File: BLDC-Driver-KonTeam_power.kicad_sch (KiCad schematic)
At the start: 73 parts, among them J1 Mode_HOA, J10 Mode_HOB, J11 Mode_LOB, J12 A, J13 B, J14 C, J2 BUck, J3 Logic_Conn, J4 Logic_Test, J5 Gate_Test, J6 IN, J7 Mode_LOC, J8 Mode_HOC, J9 Mode_LOA, Q1 IRFZ44N, Q10 IRFZ44N, Q11 IRFZ44N, Q12 IRFZ44N, Q2 IRFZ44N, Q3 IRFZ44N, Q4 IRFZ44N, Q5 IRFZ44N, Q6 IRFZ44N, Q7 IRFZ44N, Q8 IRFZ44N, Q9 IRFZ44N, U1 IR2101, U2 IR2101, U3 IR2101, U4 LM7805_TO220

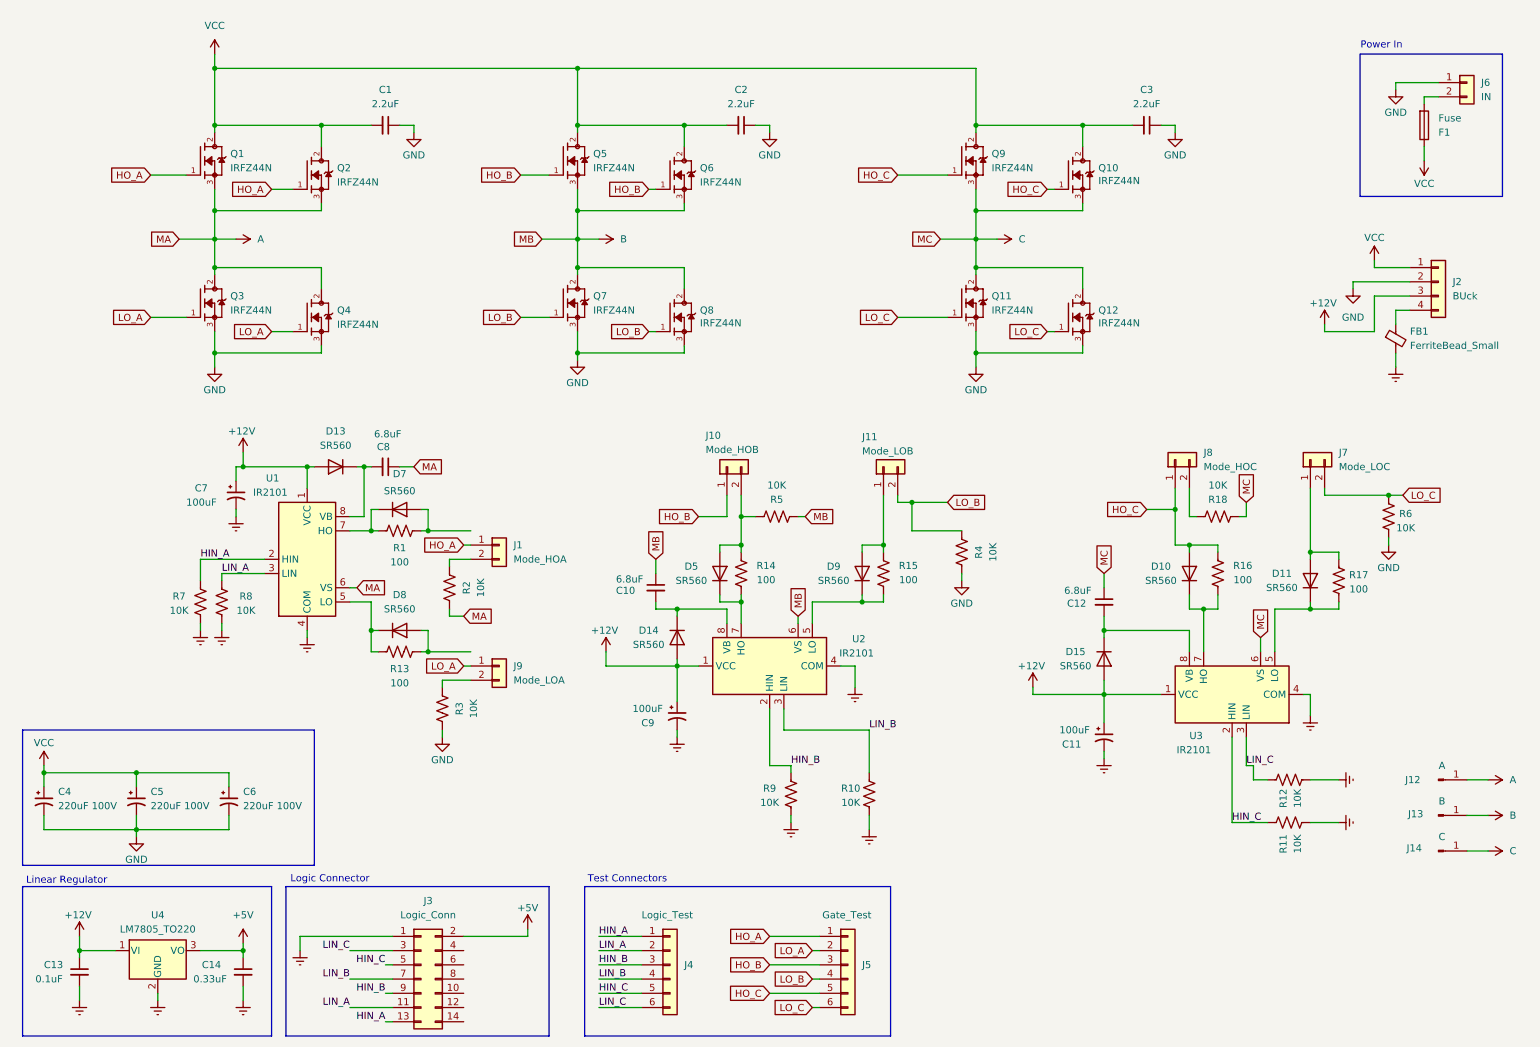
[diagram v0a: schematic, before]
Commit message: Formato Gate Drivers Enable
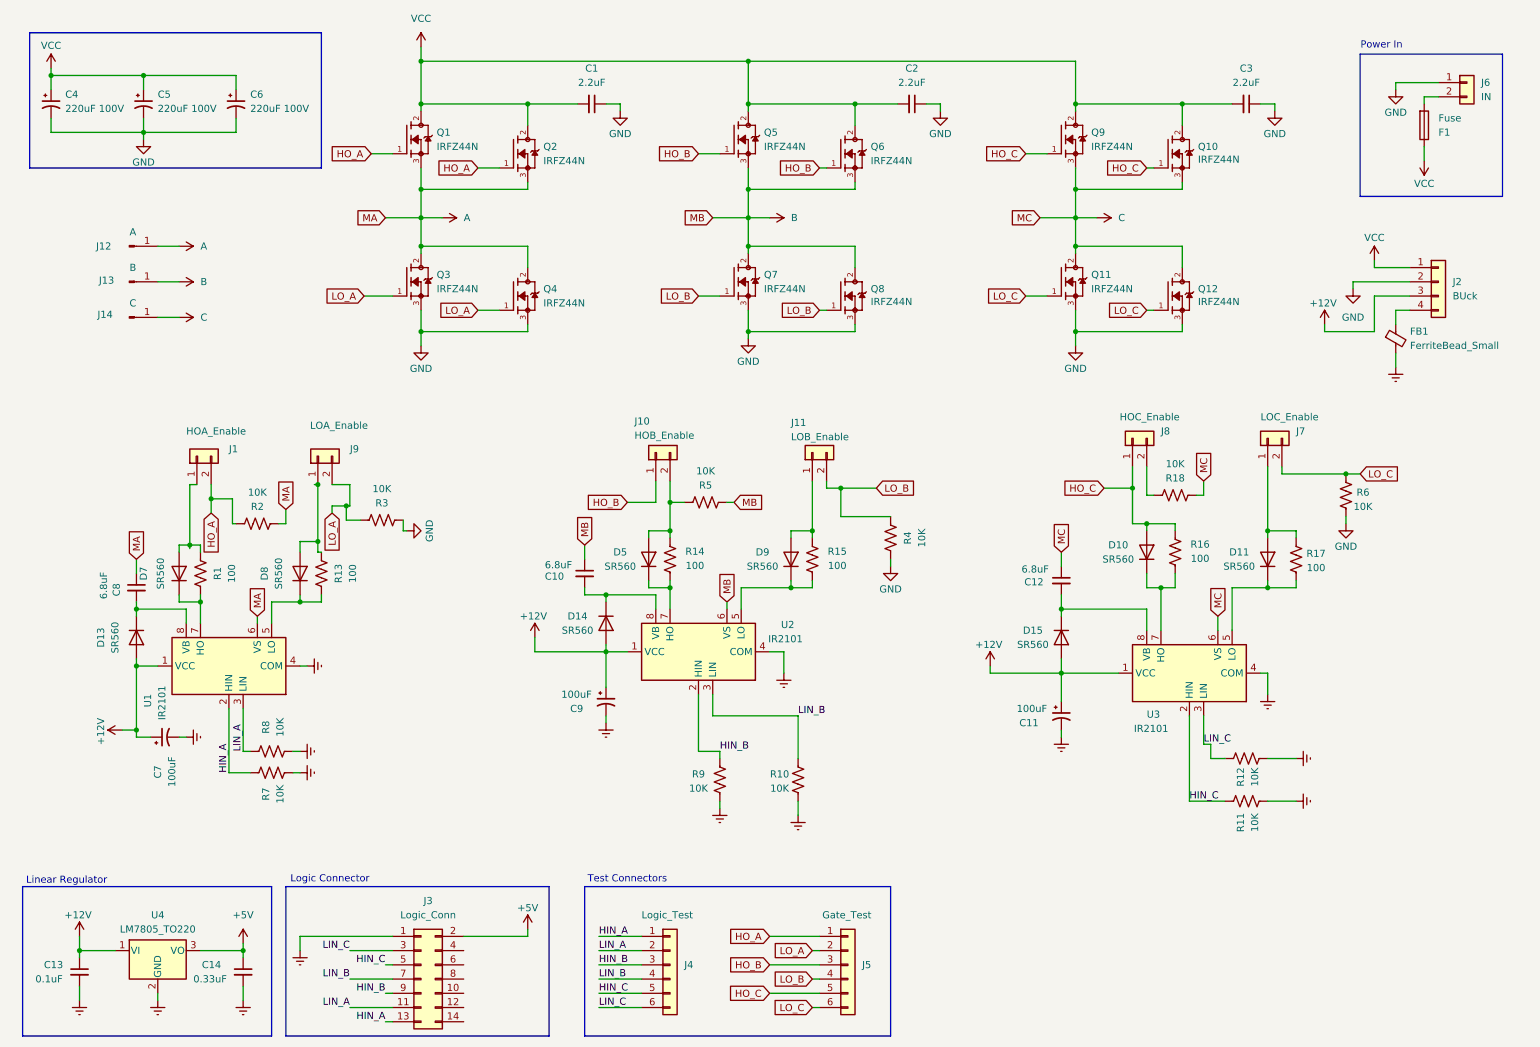
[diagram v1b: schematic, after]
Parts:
- J1: value Mode_HOA -> HOA_Enable
- J10: value Mode_HOB -> HOB_Enable
- J11: value Mode_LOB -> LOB_Enable
- J7: value Mode_LOC -> LOC_Enable
- J8: value Mode_HOC -> HOC_Enable
- J9: value Mode_LOA -> LOA_Enable
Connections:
- net HO_A: now also J1.2 (Pin_2), R2.1; no longer J1.1 (Pin_1)
- net LO_A: now also J9.2 (Pin_2), R3.1; no longer J9.1 (Pin_1)
- net at D7.2 (A), R1.1: now also J1.1 (Pin_1)
- net at D8.2 (A), R13.1: now also J9.1 (Pin_1)
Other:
- moved on the sheet: C1, C10, C11, C12, C2, C3, C4, C5, C6, C7, C8, C9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

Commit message: Refactoring the layout or the pcb. Delete the test points for the mosfet's gates , use the gate enable jumpers instead. layout of IR2021 drivers now has separated the power and the logic phases to enhance the isolation between the high power and the 12v logic. Move the LM7805 closer to the logic connector to reduce the noise and the interferences in the 5v logic. Remove the flyback diodes and the mosfets redundancy, these might be unnecesary. need to get for documentation to make sure.
Todo:
-  Investigate about the fly back diode efficency in the new mosfet
- Get calculation for the ripple supresion for the buck converter.
- remake the footprint of the buck converter.
- add the TVS diode to over voltage protection.
- calculate the heatsink distance for the mosfets. 
- make the final routing.
- get information for the 
- test point considetations
- add connector for the horn
- add holes for fix in the car
- Investigate about RC snubbers
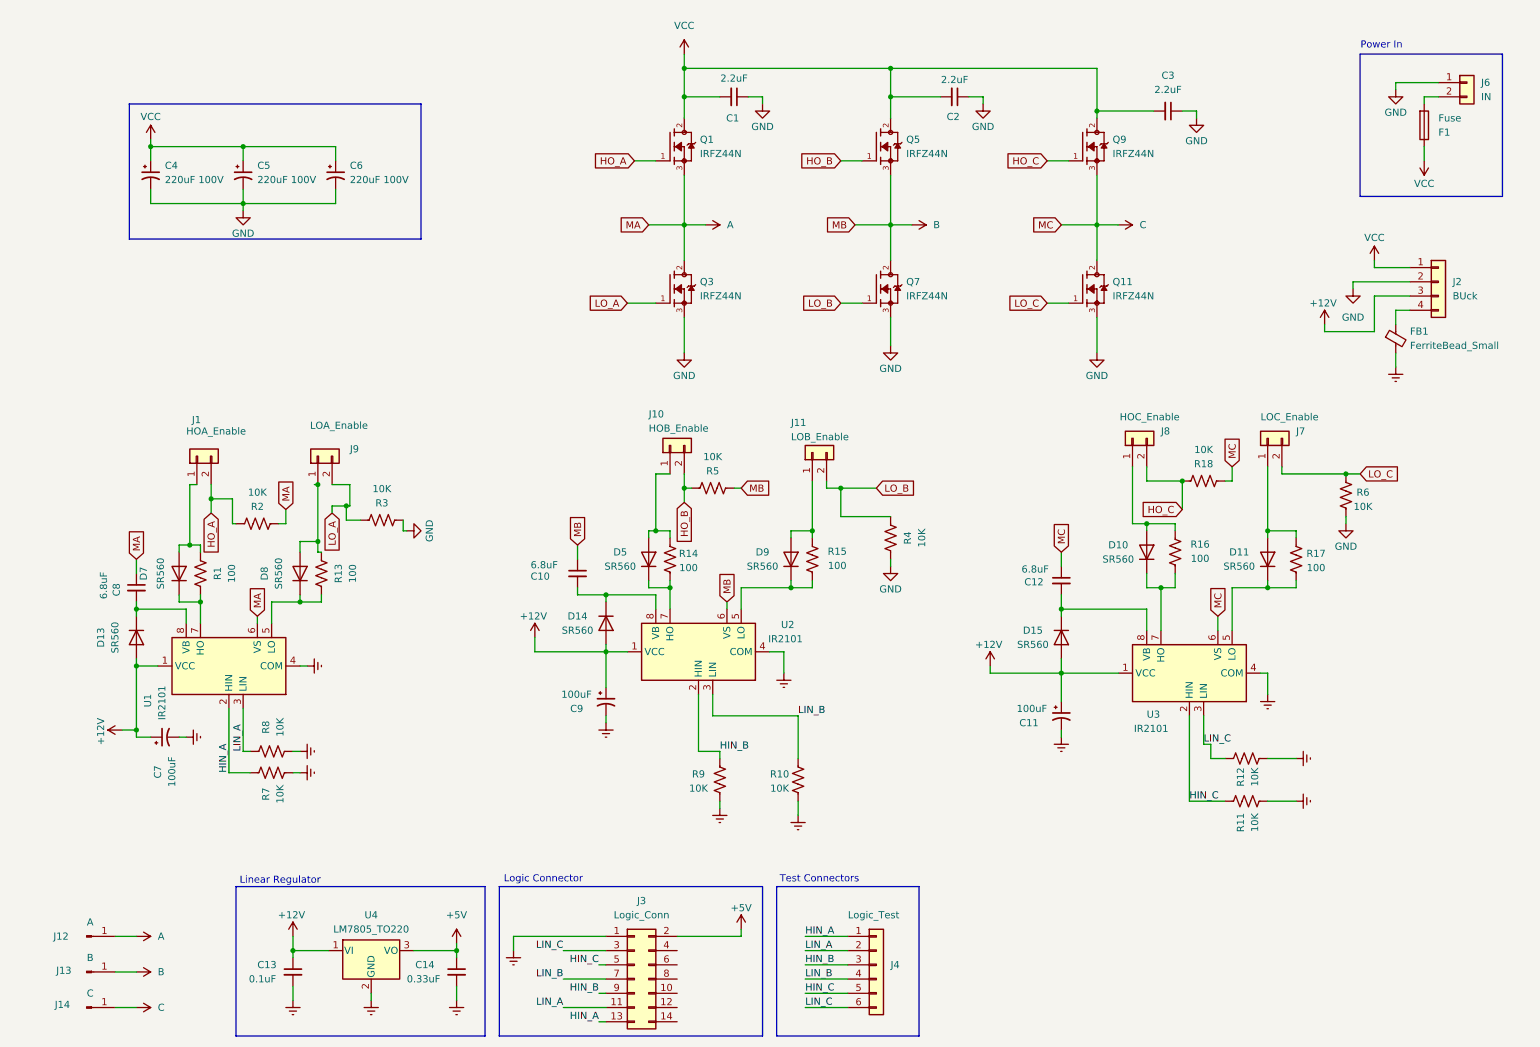
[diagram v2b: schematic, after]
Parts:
- removed J5: Gate_Test, Connector_PinSocket_2.54mm:PinSocket_1x06_P2.54mm_Vertical, symbol Connector_Generic:Conn_01x06
- removed Q10, Q12, Q2, Q4, Q6, Q8: IRFZ44N, IRFZ44N:TO254P1016X419X2286-3, symbol IRFZ44N:IRFZ44N
- J1, J10, J11, J7, J9: footprint Connector_PinHeader_2.54mm:PinHeader_1x03_P2.54mm_Vertical -> Connector_PinHeader_2.54mm:PinHeader_1x02_P2.54mm_Vertical
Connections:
- net HO_B: now also J10.2 (Pin_2), R5.1; no longer J10.1 (Pin_1)
- net HO_C: now also J8.2 (Pin_2), R18.1; no longer D10.2 (A), J8.1 (Pin_1), R16.1
- net at D5.2 (A), R14.1: now also J10.1 (Pin_1); no longer J10.2 (Pin_2), R5.1
- new net: D10.2 (A), J8.1 (Pin_1), R16.1
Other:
- moved on the sheet: C1, C10, C13, C14, C2, C3, C4, C5, C6, J10, J12, J13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

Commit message: - Added Footprint Buck converter - Add TVS diode for over voltage protection - Routed tracks (need confirmation) - Add conector for the horn, need to add specific connector - Added .step format for the mecanical considerations
Todo:
- add holes to fix to the car structure
- Make specific connector for the horn
- Calculate heatsink spacing
- Investigate about RC snubbers
- Investigate about the fly back diode efficency in the new mosfet
- Make the proyect has the embebed libraries for buck converter, mosfets, 
- Add Documentation Folder. (Datasheets, comparation sheets , etc)
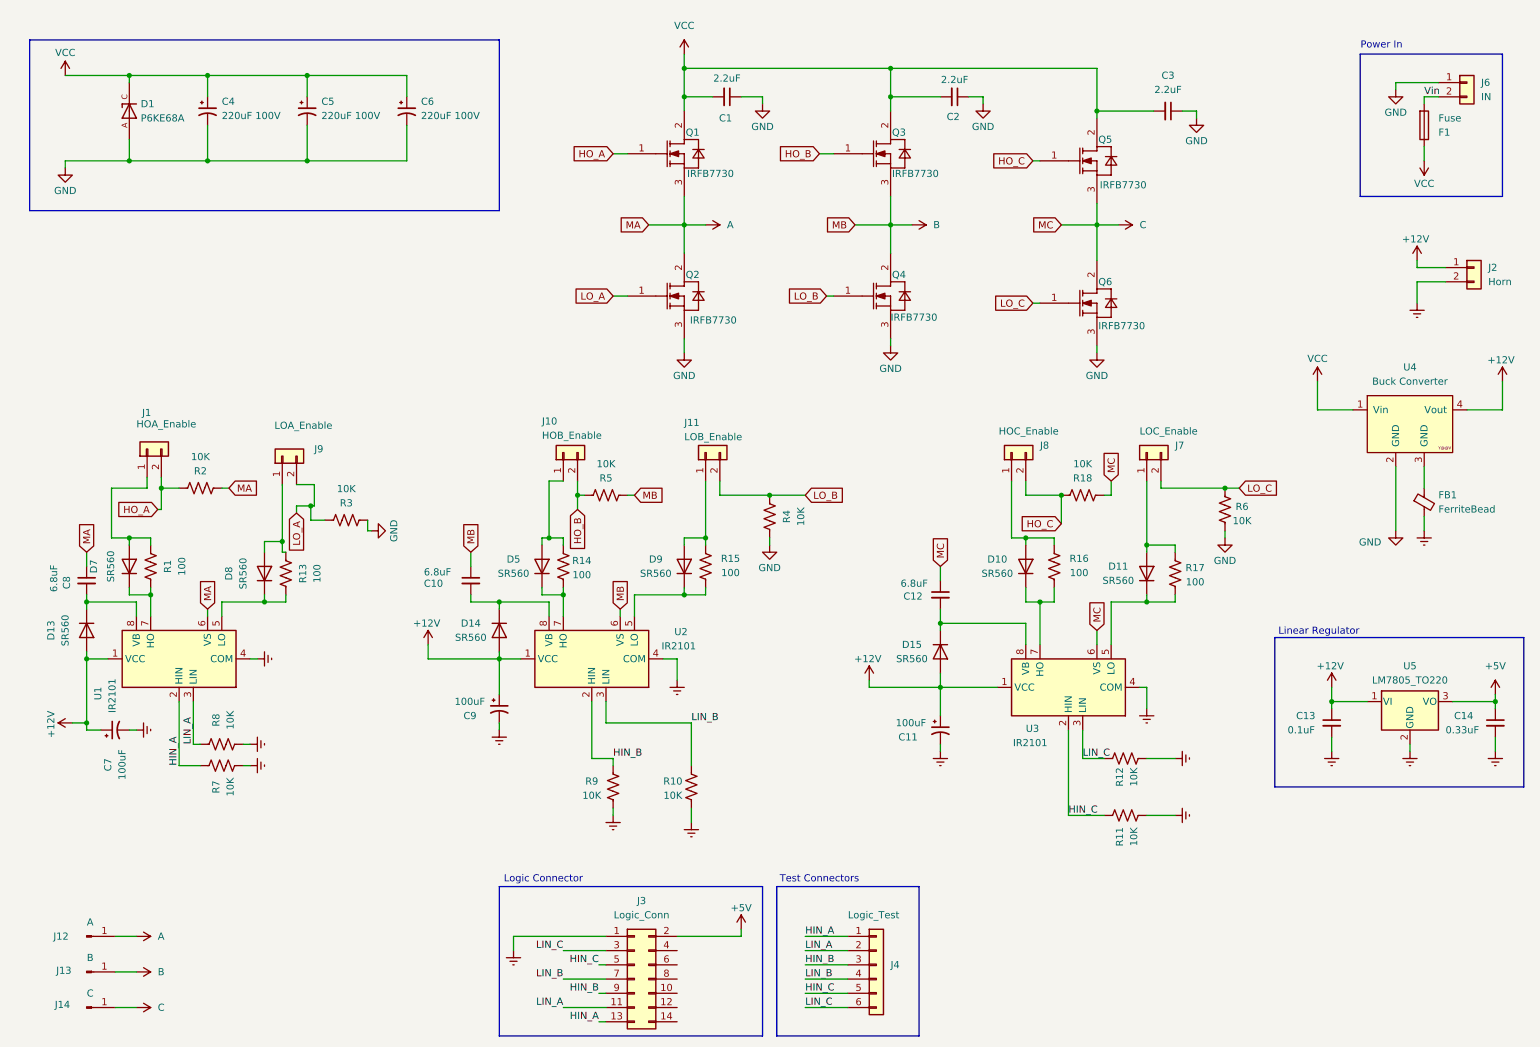
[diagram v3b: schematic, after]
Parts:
- removed J2: BUck, DC_DC_LM2596_small:DC_DC_LM2596_small, symbol Connector_Generic:Conn_01x04
- added D1: P6KE68A, P6KE68A:DIOAD1300W80L670D310, symbol P6KE68A:P6KE68A
- added J2: Horn, Connector_AMASS:AMASS_XT60-F_1x02_P7.20mm_Vertical, symbol Connector_Generic:Conn_01x02
- added U4: Buck Converter, KiCad:YAAJ_DCDC_StepDown_LM2596, symbol yaaj_dcdc_stepdown_lm2596:YAAJ_DCDC_StepDown_LM2596
- FB1: value FerriteBead_Small -> FerriteBead
- Q1: value IRFZ44N -> IRFB7730; footprint IRFZ44N:TO254P1016X419X2286-3 -> kicad:IRFB7730; symbol IRFZ44N:IRFZ44N -> IRFB7730:IRFB7730; Manufacturer (none) -> Infineon Technologies; Manufacturer Order Number (none) -> IRFB7730; PackageReference (none) -> PG-TO220-3-904
- Q2: renamed from Q3; value IRFZ44N -> IRFB7730; footprint IRFZ44N:TO254P1016X419X2286-3 -> kicad:IRFB7730; symbol IRFZ44N:IRFZ44N -> IRFB7730:IRFB7730; Manufacturer (none) -> Infineon Technologies; Manufacturer Order Number (none) -> IRFB7730; PackageReference (none) -> PG-TO220-3-904
- Q3: renamed from Q5; value IRFZ44N -> IRFB7730; footprint IRFZ44N:TO254P1016X419X2286-3 -> kicad:IRFB7730; symbol IRFZ44N:IRFZ44N -> IRFB7730:IRFB7730; Manufacturer (none) -> Infineon Technologies; Manufacturer Order Number (none) -> IRFB7730; PackageReference (none) -> PG-TO220-3-904
- Q4: renamed from Q7; value IRFZ44N -> IRFB7730; footprint IRFZ44N:TO254P1016X419X2286-3 -> kicad:IRFB7730; symbol IRFZ44N:IRFZ44N -> IRFB7730:IRFB7730; Manufacturer (none) -> Infineon Technologies; Manufacturer Order Number (none) -> IRFB7730; PackageReference (none) -> PG-TO220-3-904
- Q5: renamed from Q9; value IRFZ44N -> IRFB7730; footprint IRFZ44N:TO254P1016X419X2286-3 -> kicad:IRFB7730; symbol IRFZ44N:IRFZ44N -> IRFB7730:IRFB7730; Manufacturer (none) -> Infineon Technologies; Manufacturer Order Number (none) -> IRFB7730; PackageReference (none) -> PG-TO220-3-904
- Q6: renamed from Q11; value IRFZ44N -> IRFB7730; footprint IRFZ44N:TO254P1016X419X2286-3 -> kicad:IRFB7730; symbol IRFZ44N:IRFZ44N -> IRFB7730:IRFB7730; Manufacturer (none) -> Infineon Technologies; Manufacturer Order Number (none) -> IRFB7730; PackageReference (none) -> PG-TO220-3-904
- renumbered U4 to U5
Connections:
- net +12V: now also J2.1 (Pin_1), U4.4 (Vout)
- net Earth: now also J2.2 (Pin_2)
- net GND: now also D1.A, U4.2 (GND)
- net VCC: now also D1.C, U4.1 (Vin)
- net Vin: now reaches F1.2, J6.2 (Pin_2)
- net at FB1.1: now also U4.3 (GND)
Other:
- moved on the sheet: C1, C10, C11, C12, C13, C14, C4, C5, C6, C7, C8, C9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
